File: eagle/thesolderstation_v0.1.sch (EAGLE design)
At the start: 47 parts, among them IC1 OPA336U, IC2 78L05F, J1 POWER_JACKPTH, J2 AVR_SPI_PRG_6NS, T1 IRF7416, T2 BSN20, T3 BSN20, U1 ATMEGA328P, U2 FT232RLSSOP, Y1 16MHZ

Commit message: Switched display's DC and CS pins for better routing
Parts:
- removed U$8: OSH_LOGOS, Logos:OSH_LOGOS
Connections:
- net CS: now also U1.PB1(OC1A); no longer U1.PB2(SS/OC1B)
- net DC: now also U1.PB2(SS/OC1B); no longer U1.PB1(OC1A)
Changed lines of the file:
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@@
 <?xml version="1.0" encoding="utf-8"?>
 <!DOCTYPE eagle SYSTEM "eagle.dtd">
-<eagle version="7.4.0">
+<eagle version="6.6.0">
 <drawing>
 <settings>
@@
 <part name="C5" library="rcl" deviceset="C-EU" device="C0603" value="100n"/>
 <part name="R11" library="rcl" deviceset="R-EU_" device="R0603" value="10k"/>
-<part name="U$8" library="Logos" deviceset="OSH_LOGO" device="S"/>
 <part name="U$2" library="Matthias" deviceset="AUDIO_JACK_3,5MM" device="CONRAD"/>
 <part name="P+10" library="supply" deviceset="+5V" device=""/>
@@
 <instance part="C5" gate="G$1" x="160.02" y="30.48"/>
 <instance part="R11" gate="G$1" x="152.4" y="96.52" rot="R270"/>
-<instance part="U$8" gate="G$1" x="314.96" y="96.52"/>
 <instance part="U$2" gate="G$1" x="330.2" y="218.44" rot="MR0"/>
 <instance part="P+10" gate="1" x="309.88" y="160.02"/>
@@
 </segment>
 <segment>
+<pinref part="U1" gate="G$1" pin="PB1(OC1A)"/>
+<wire x1="91.44" y1="93.98" x2="101.6" y2="93.98" width="0.1524" layer="91"/>
+<label x="96.52" y="93.98" size="1.778" layer="95"/>
+</segment>
+</net>
+<net name="DC" class="0">
+<segment>
+<pinref part="R8" gate="G$1" pin="1"/>
+<wire x1="322.58" y1="147.32" x2="314.96" y2="147.32" width="0.1524" layer="91"/>
+<label x="314.96" y="147.32" size="1.778" layer="95"/>
+</segment>
+<segment>
 <pinref part="U1" gate="G$1" pin="PB2(SS/OC1B)"/>
 <wire x1="91.44" y1="91.44" x2="101.6" y2="91.44" width="0.1524" layer="91"/>
@@
 </segment>
 </net>
-<net name="DC" class="0">
-<segment>
-<pinref part="R8" gate="G$1" pin="1"/>
-<wire x1="322.58" y1="147.32" x2="314.96" y2="147.32" width="0.1524" layer="91"/>
-<label x="314.96" y="147.32" size="1.778" layer="95"/>
-</segment>
-<segment>
-<pinref part="U1" gate="G$1" pin="PB1(OC1A)"/>
-<wire x1="91.44" y1="93.98" x2="101.6" y2="93.98" width="0.1524" layer="91"/>
-<label x="96.52" y="93.98" size="1.778" layer="95"/>
-</segment>
-</net>

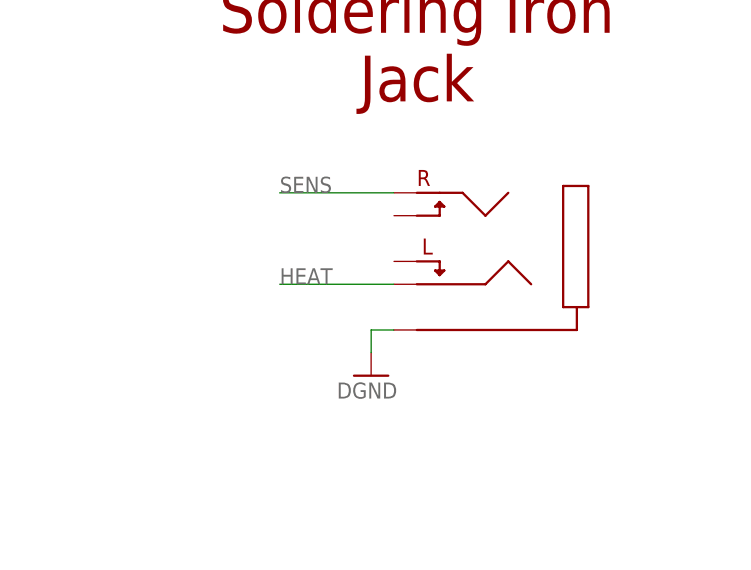
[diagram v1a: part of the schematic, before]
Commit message: Switched to a different 3.5mm soldering iron jack as current rating was too low (0.5A).
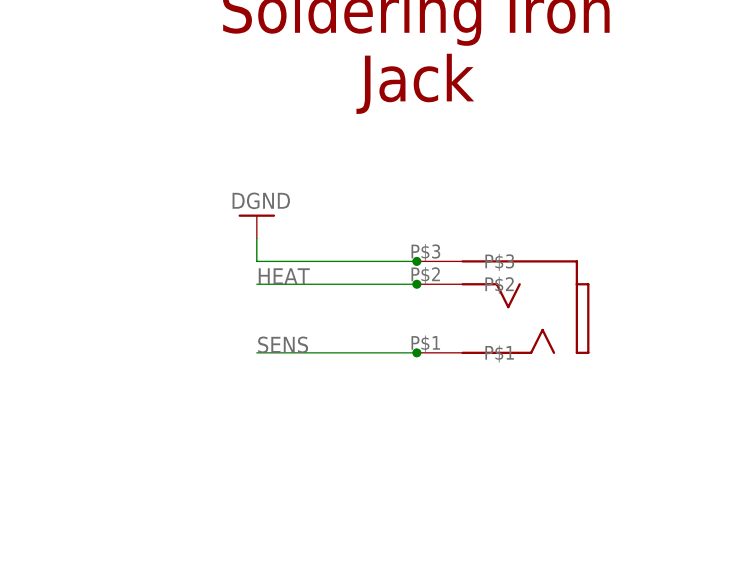
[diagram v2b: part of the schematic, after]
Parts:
- removed U$2: AUDIO_JACK_3,5MMCONRAD, Matthias:AUDIO_JACK_3,5MMCONRAD
- added U$1: 35RASMT2BHNTRX, alvarop-lib:35RASMT2BHNTRX
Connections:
- net DGND: now also U$1.P$3; no longer U$2.P$5
- net HEAT: now also U$1.P$2; no longer U$2.P$4
- net SENS: now also U$1.P$1; no longer U$2.P$1
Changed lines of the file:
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@@
 <part name="C5" library="rcl" deviceset="C-EU" device="C0603" value="100n"/>
 <part name="R11" library="rcl" deviceset="R-EU_" device="R0603" value="10k"/>
-<part name="U$2" library="Matthias" deviceset="AUDIO_JACK_3,5MM" device="CONRAD"/>
 <part name="P+10" library="supply" deviceset="+5V" device=""/>
 <part name="R13" library="rcl" deviceset="R-EU_" device="R0603" value="1M"/>
@@
 <part name="R22" library="rcl" deviceset="R-EU_" device="R0603" value="10k"/>
 <part name="P+7" library="supply" deviceset="+5V" device=""/>
+<part name="U$1" library="alvarop-lib" deviceset="35RASMT2BHNTRX" device=""/>
 </parts>
 <sheets>
@@
 <instance part="C7" gate="G$1" x="139.7" y="30.48"/>
 <instance part="P+6" gate="1" x="109.22" y="40.64"/>
-<instance part="GND6" gate="1" x="322.58" y="200.66"/>
+<instance part="GND6" gate="1" x="309.88" y="218.44" rot="R180"/>
 <instance part="P+4" gate="1" x="185.42" y="142.24"/>
 <instance part="JP2" gate="G$1" x="93.98" y="45.72" smashed="yes" rot="R270">
@@
 <instance part="C5" gate="G$1" x="160.02" y="30.48"/>
 <instance part="R11" gate="G$1" x="152.4" y="96.52" rot="R270"/>
-<instance part="U$2" gate="G$1" x="330.2" y="218.44" rot="MR0"/>
 <instance part="P+10" gate="1" x="309.88" y="160.02"/>
 <instance part="R13" gate="G$1" x="33.02" y="220.98" rot="R270"/>
@@
 <instance part="R22" gate="G$1" x="246.38" y="66.04" rot="R90"/>
 <instance part="P+7" gate="1" x="246.38" y="55.88" rot="R180"/>
+<instance part="U$1" gate="G$1" x="337.82" y="208.28" rot="R180"/>
 </instances>
 <busses>
@@
 </segment>
 <segment>
-<wire x1="325.12" y1="205.74" x2="322.58" y2="205.74" width="0.1524" layer="91"/>
-<wire x1="322.58" y1="205.74" x2="322.58" y2="203.2" width="0.1524" layer="91"/>
+<wire x1="327.66" y1="213.36" x2="309.88" y2="213.36" width="0.1524" layer="91"/>
+<wire x1="309.88" y1="213.36" x2="309.88" y2="215.9" width="0.1524" layer="91"/>
 <pinref part="GND6" gate="1" pin="DGND"/>
-<pinref part="U$2" gate="G$1" pin="P$5"/>
+<pinref part="U$1" gate="G$1" pin="P$3"/>
+<junction x="327.66" y="213.36"/>
 </segment>
 <segment>
@@
 </segment>
 <segment>
-<wire x1="325.12" y1="220.98" x2="312.42" y2="220.98" width="0.1524" layer="91"/>
-<label x="312.42" y="220.98" size="1.778" layer="95"/>
-<pinref part="U$2" gate="G$1" pin="P$1"/>
+<wire x1="327.66" y1="203.2" x2="309.88" y2="203.2" width="0.1524" layer="91"/>
+<label x="309.88" y="203.2" size="1.778" layer="95"/>
+<pinref part="U$1" gate="G$1" pin="P$1"/>
+<junction x="327.66" y="203.2"/>
 </segment>
 </net>
@@
 <net name="HEAT" class="0">
 <segment>
-<pinref part="U$2" gate="G$1" pin="P$4"/>
-<wire x1="312.42" y1="210.82" x2="325.12" y2="210.82" width="0.1524" layer="91"/>
-<label x="312.42" y="210.82" size="1.778" layer="95"/>
-</segment>
-<segment>
+<wire x1="309.88" y1="210.82" x2="327.66" y2="210.82" width="0.1524" layer="91"/>
+<label x="309.88" y="210.82" size="1.778" layer="95"/>
+<pinref part="U$1" gate="G$1" pin="P$2"/>
+<junction x="327.66" y="210.82"/>
+</segment>
+<segment>
